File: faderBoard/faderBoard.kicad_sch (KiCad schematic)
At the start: 4 parts

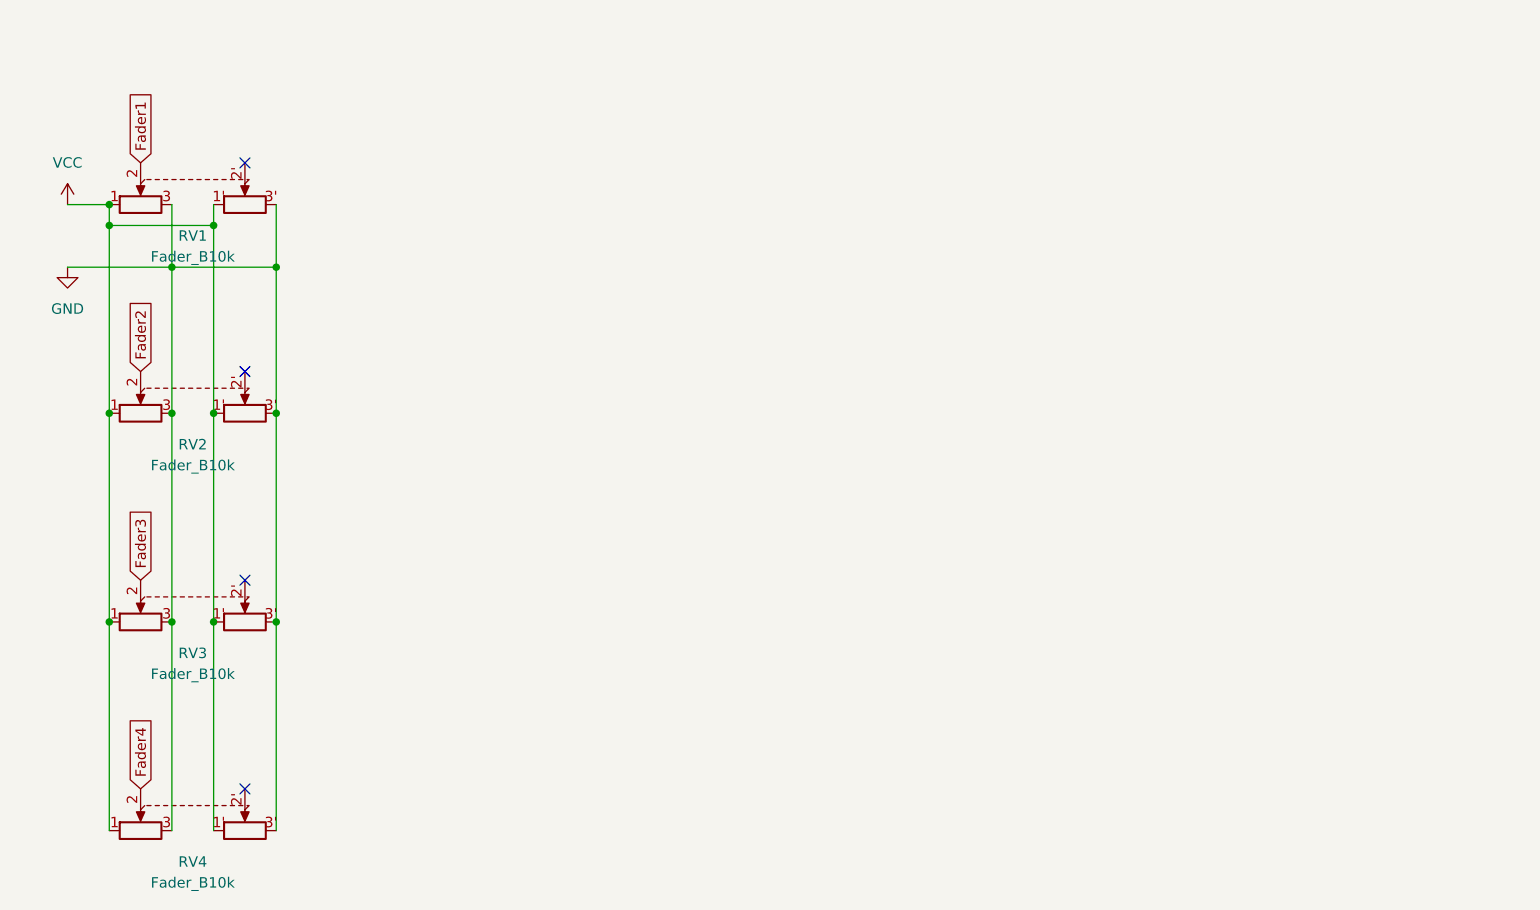
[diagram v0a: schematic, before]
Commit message: added pinHeaders
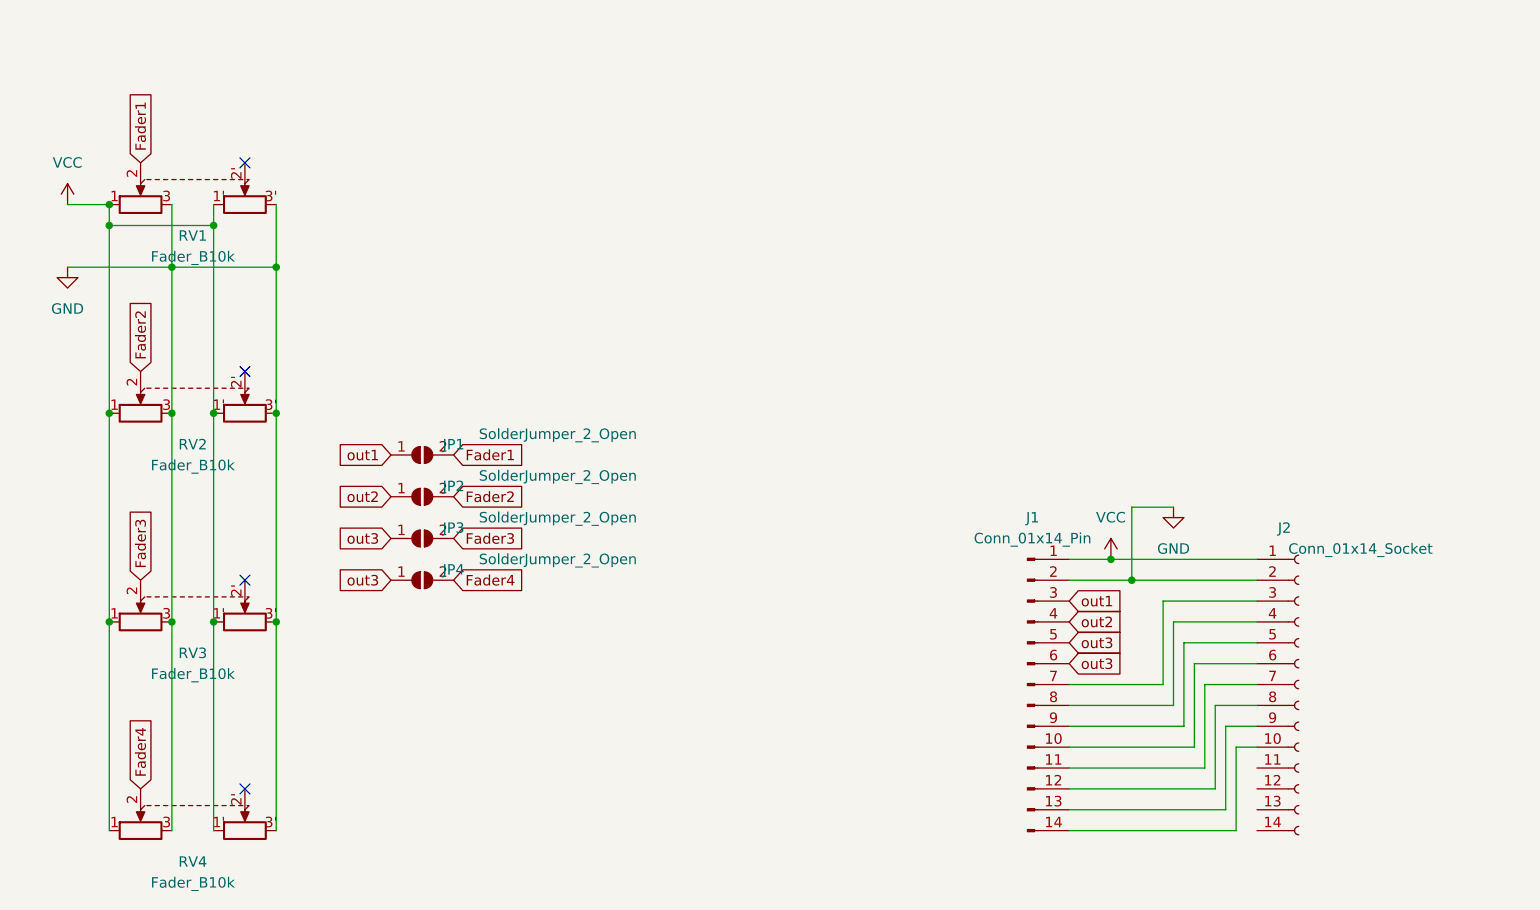
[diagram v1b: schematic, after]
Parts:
- added J1: Conn_01x14_Pin, symbol Connector:Conn_01x14_Pin
- added J2: Conn_01x14_Socket, symbol Connector:Conn_01x14_Socket
- added JP1, JP2, JP3, JP4: SolderJumper_2_Open, symbol Jumper:SolderJumper_2_Open
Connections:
- net Fader1: now also JP1.2 (B)
- net Fader2: now also JP2.2 (B)
- net Fader3: now also JP3.2 (B)
- net Fader4: now also JP4.2 (B)
- net GND: now also J1.2 (Pin_2), J2.2 (Pin_2)
- net VCC: now also J1.1 (Pin_1), J2.1 (Pin_1)
- new net: J1.14 (Pin_14), J2.10 (Pin_10)
- new net: J1.7 (Pin_7), J2.3 (Pin_3)
- new net: J1.8 (Pin_8), J2.4 (Pin_4)
- new net: J1.9 (Pin_9), J2.5 (Pin_5)
- new net: J1.10 (Pin_10), J2.6 (Pin_6)
- new net: J1.11 (Pin_11), J2.7 (Pin_7)
- new net: J1.12 (Pin_12), J2.8 (Pin_8)
- new net: J1.13 (Pin_13), J2.9 (Pin_9)
- new net out1: J1.3 (Pin_3), JP1.1 (A)
- new net out2: J1.4 (Pin_4), JP2.1 (A)
- new net out3: J1.5 (Pin_5), J1.6 (Pin_6), JP3.1 (A), JP4.1 (A)

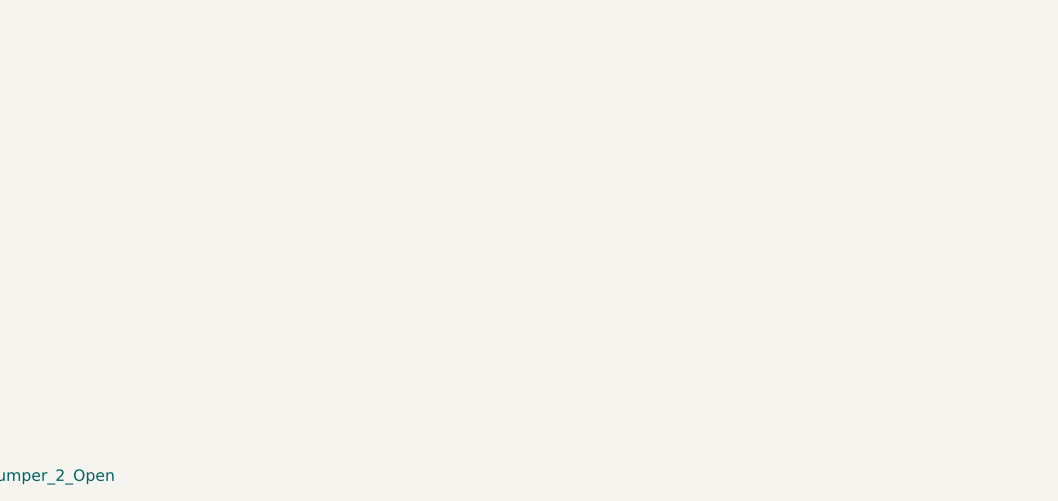
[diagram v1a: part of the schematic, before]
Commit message: added ADC
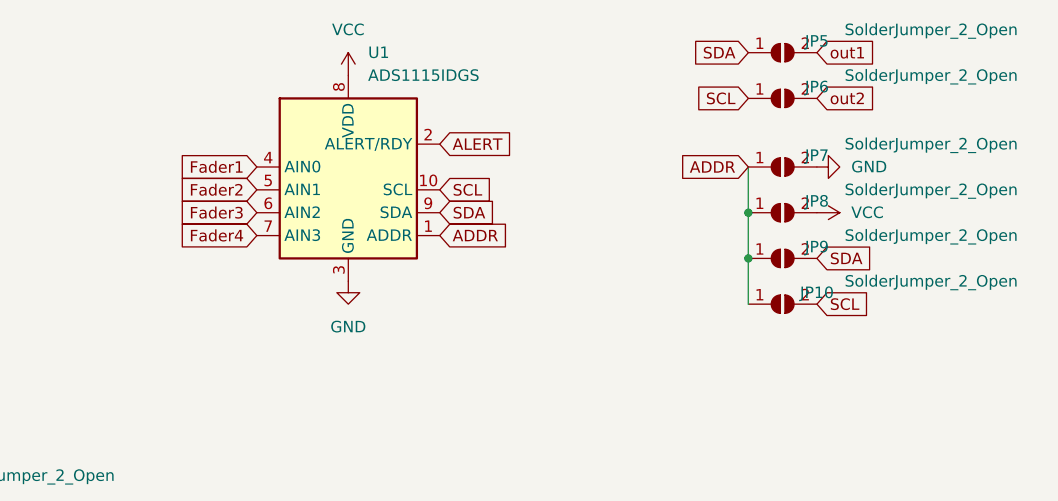
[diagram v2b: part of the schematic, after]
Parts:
- added JP10, JP5, JP6, JP7, JP8, JP9: SolderJumper_2_Open, symbol Jumper:SolderJumper_2_Open
- added U1: ADS1115IDGS, Package_SO:TSSOP-10_3x3mm_P0.5mm, symbol Analog_ADC:ADS1115IDGS
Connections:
- net Fader1: now also U1.4 (AIN0)
- net Fader2: now also U1.5 (AIN1)
- net Fader3: now also U1.6 (AIN2)
- net Fader4: now also U1.7 (AIN3)
- net GND: now also JP7.2 (B), U1.3 (GND)
- net VCC: now also JP8.2 (B), U1.8 (VDD)
- net out1: now also JP5.2 (B)
- net out2: now also JP6.2 (B)
- new net ADDR: JP10.1 (A), JP7.1 (A), JP8.1 (A), JP9.1 (A), U1.1 (ADDR)
- new net ALERT: U1.2 (ALERT/RDY)
- new net SCL: JP10.2 (B), JP6.1 (A), U1.10 (SCL)
- new net SDA: JP5.1 (A), JP9.2 (B), U1.9 (SDA)

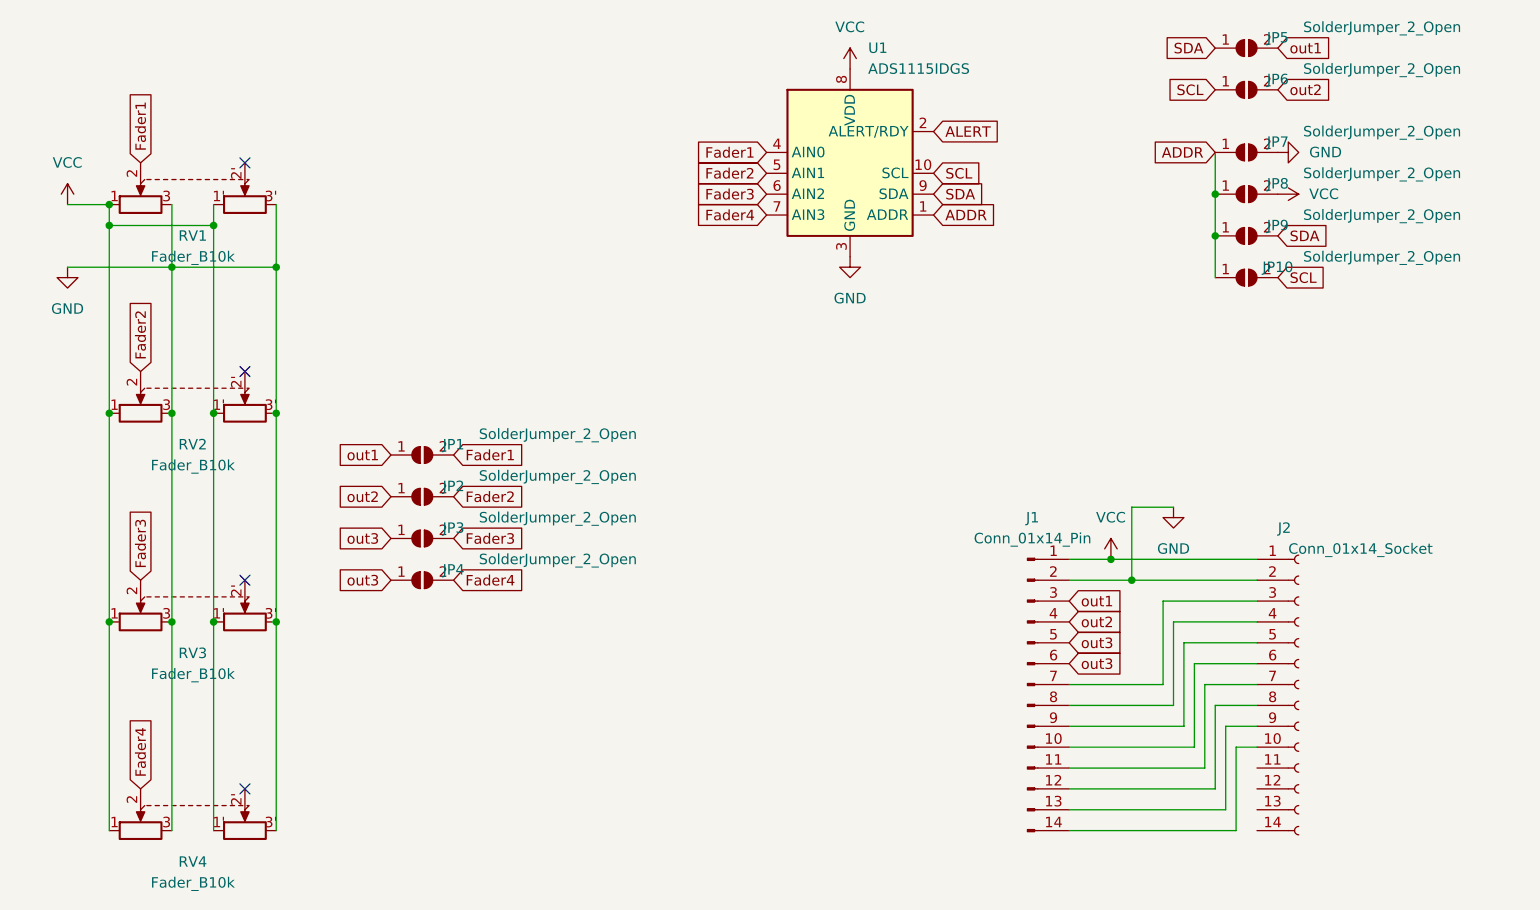
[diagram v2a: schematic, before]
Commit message: added capacitors
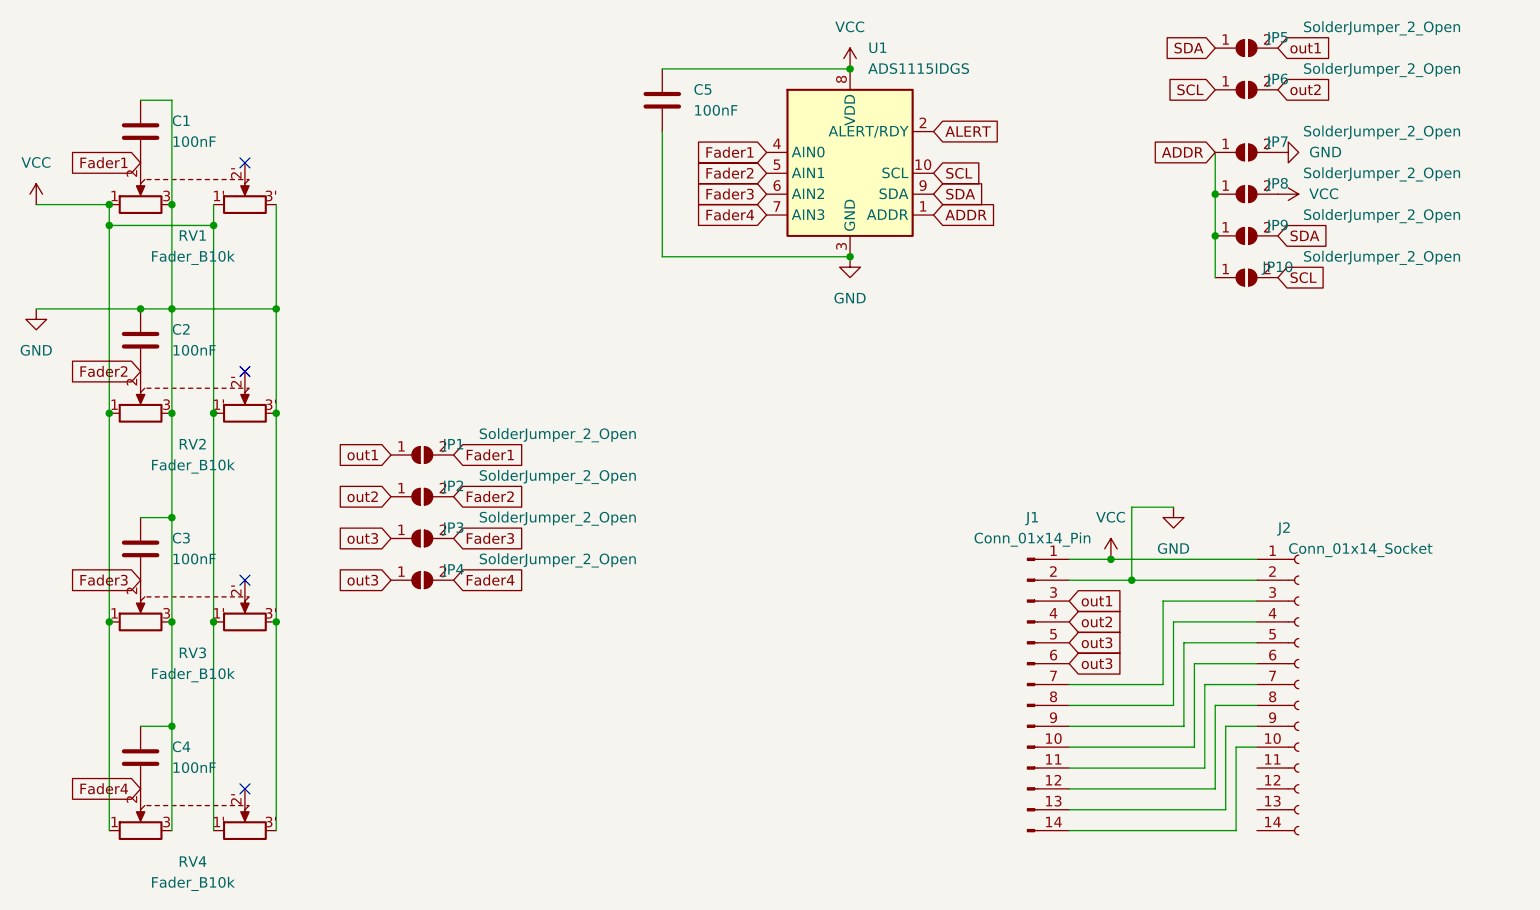
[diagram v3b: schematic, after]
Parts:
- added C1, C2, C3, C4, C5: 100nF, symbol Device:C
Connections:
- net Fader1: now also C1.2
- net Fader2: now also C2.2
- net Fader3: now also C3.2
- net Fader4: now also C4.2
- net GND: now also C1.1, C2.1, C3.1, C4.1, C5.2
- net VCC: now also C5.1

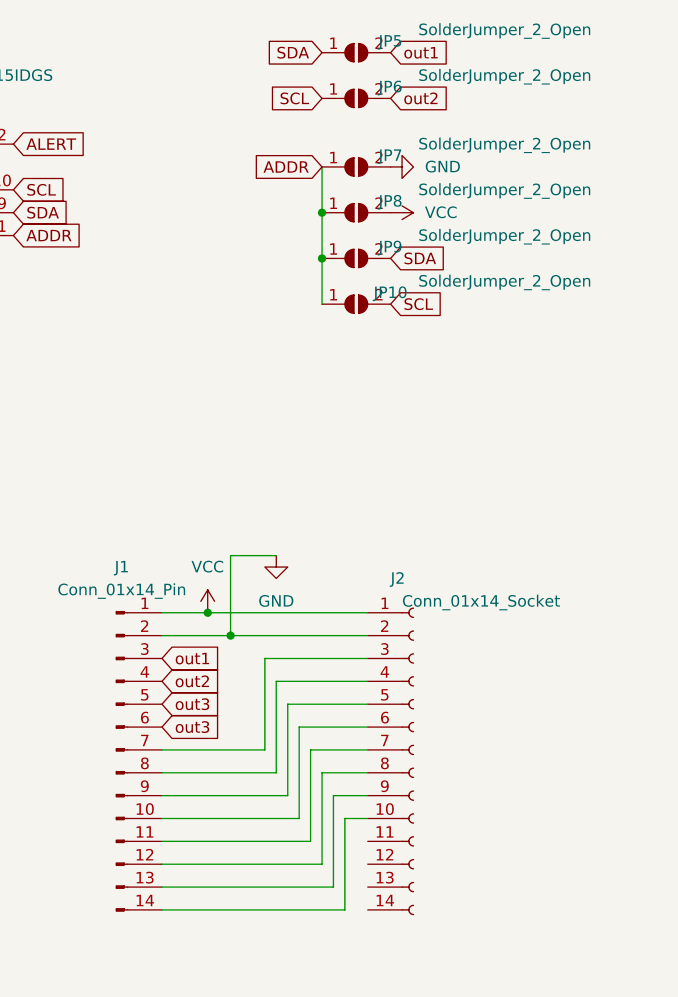
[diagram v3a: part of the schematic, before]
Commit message: added in i2c connenciton
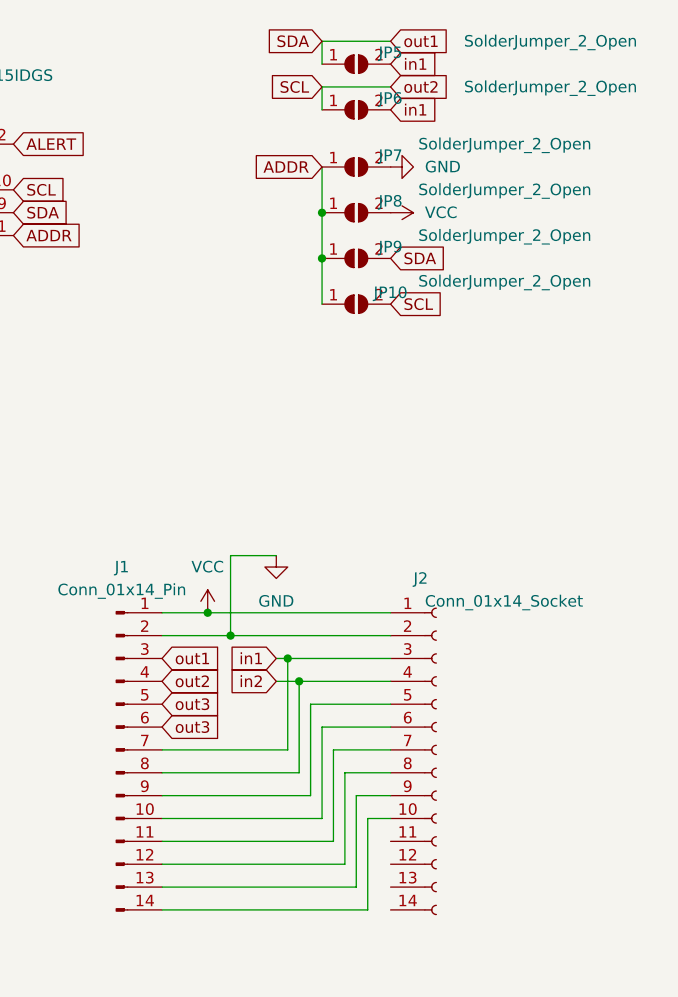
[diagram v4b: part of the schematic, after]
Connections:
- net SCL: now also J1.4 (Pin_4), JP2.1 (A)
- net SDA: now also J1.3 (Pin_3), JP1.1 (A)
- net in1: now reaches J1.7 (Pin_7), J2.3 (Pin_3)
- net in1: now also JP5.2 (B), JP6.2 (B)
- net in2: now reaches J1.8 (Pin_8), J2.4 (Pin_4)
- removed net out1: J1.3 (Pin_3), JP1.1 (A), JP5.2 (B)
- removed net out2: J1.4 (Pin_4), JP2.1 (A), JP6.2 (B)
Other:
- moved on the sheet: J2
